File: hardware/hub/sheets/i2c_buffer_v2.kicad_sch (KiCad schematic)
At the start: 14 parts, among them J2 Conn_01x02, J201 RJHSE5380, J202 RJHSE5380, J203 Qwiic, U201 PCA9615

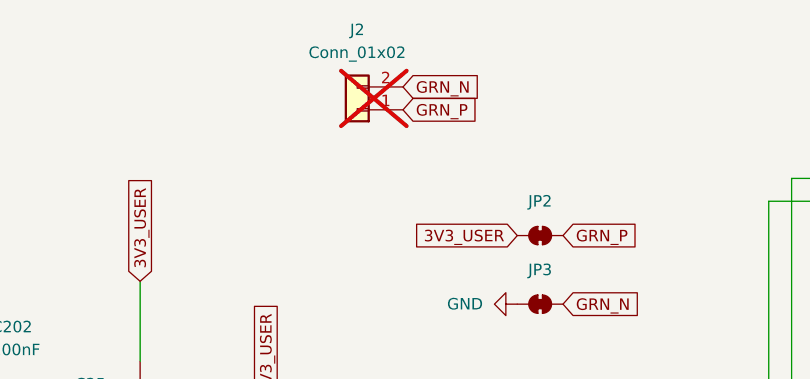
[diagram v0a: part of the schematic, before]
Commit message: hardware(hub): J2 gets a 3V3_SYS pin next to VCC_2, docs explain why
J2 (VCC_2 INJ) grows from two pins to three: GRN_N, VCC_2 and the always-on
3V3_SYS rail. A jumper from 3V3_SYS to VCC_2 feeds a second satellite from the
hub, and the pin lets test clips power the board at 3.3 V instead of USB.

The header moves and is rotated, with its routing and zones updated.
The buffer module doc describes the pinout and both uses, and warns to cut
JP2 first. Neither use is tested yet.
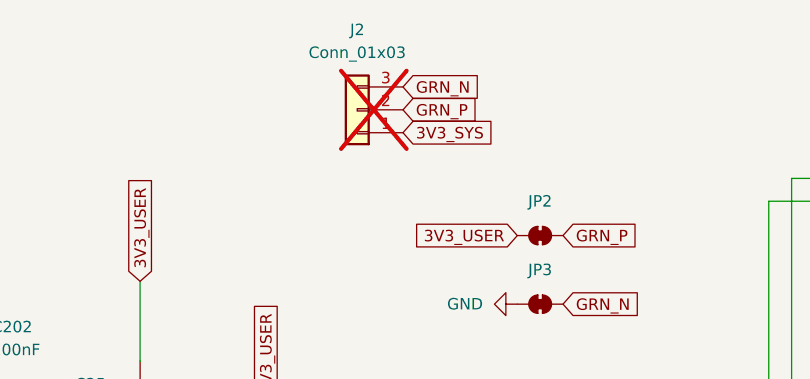
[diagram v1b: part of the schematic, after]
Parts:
- J2: value Conn_01x02 -> Conn_01x03; footprint Connector_PinHeader_2.54mm:PinHeader_1x02_P2.54mm_Vertical -> Connector_PinHeader_2.54mm:PinHeader_1x03_P2.54mm_Vertical; symbol Connector_Generic:Conn_01x02 -> Connector_Generic:Conn_01x03
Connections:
- net GRN_N: now also J2.3 (Pin_3); no longer J2.2 (Pin_2)
- net GRN_P: now also J2.2 (Pin_2); no longer J2.1 (Pin_1)
- new net 3V3_SYS: J2.1 (Pin_1)
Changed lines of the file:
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@@
 		)
 	)
+	(global_label "3V3_SYS"
+		(shape input)
+		(at 139.7 41.91 0)
+		(fields_autoplaced yes)
+		(effects
+			(font
+				(size 1.27 1.27)
+			)
+			(justify left)
+		)
+		(property "Intersheetrefs" "${INTERSHEET_REFS}"
+			(at 150.668 41.91 0)
+			(hide yes)
+			(show_name no)
+			(do_not_autoplace no)
+			(effects
+				(font
+					(size 1.27 1.27)
+				)
+				(justify left)
+			)
+		)
+	)
 	(global_label "3V3_USER"
 		(shape input)
@@
 	)
 	(symbol
-		(lib_id "Connector_Generic:Conn_01x02")
+		(lib_id "Connector_Generic:Conn_01x03")
 		(at 134.62 39.37 180)
 		(unit 1)
@@
 			)
 		)
-		(property "Value" "Conn_01x02"
+		(property "Value" "Conn_01x03"
 			(at 134.62 33.02 0)
 			(show_name no)
@@
 			)
 		)
-		(property "Footprint" "Connector_PinHeader_2.54mm:PinHeader_1x02_P2.54mm_Vertical"
+		(property "Footprint" "Connector_PinHeader_2.54mm:PinHeader_1x03_P2.54mm_Vertical"
 			(at 134.62 39.37 0)
 			(hide yes)
@@
 		(pin "1"
 		)
+		(pin "3"
+		)
 		(instances
